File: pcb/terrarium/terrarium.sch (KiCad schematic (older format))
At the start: 11 parts

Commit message: add support for old pcb, add final changes to pcb
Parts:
- added i2c3: Extra_5v, Connector_PinHeader_2.54mm:PinHeader_1x04_P2.54mm_Vertical, symbol Connector_Generic:Conn_01x04
- added i2c4: Extra_3v3, Connector_PinHeader_2.54mm:PinHeader_1x04_P2.54mm_Vertical, symbol Connector_Generic:Conn_01x04
- added rxtx1: Conn_01x02, Connector_PinSocket_2.54mm:PinSocket_1x02_P2.54mm_Vertical, symbol Connector_Generic:Conn_01x02
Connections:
- net 3v3: now also i2c4.2 (Pin_2)
- net GND: now also i2c3.1 (Pin_1), i2c4.1 (Pin_1)
- net SCL: now also i2c3.4 (Pin_4), i2c4.4 (Pin_4)
- net SDA: now also i2c3.3 (Pin_3), i2c4.3 (Pin_3)
- net VCC: now also i2c3.2 (Pin_2)
- net RX: now reaches esp32-left1.15 (Pin_15)
- net RX: now also rxtx1.1 (Pin_1)
- net TX: now reaches esp32-left1.16 (Pin_16)
- net TX: now also rxtx1.2 (Pin_2)
- no-connect marks 34 -> 32
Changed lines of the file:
@@
-$EndComp
-$Comp
-L Connector_Generic:Conn_01x04 i2c2
-U 1 1 618742D4
-P 1550 1950
-F 0 "i2c2" H 1630 1942 50  0000 L CNN
-F 1 "LCD" H 1630 1851 50  0000 L CNN
-F 2 "Connector_PinHeader_2.54mm:PinHeader_1x04_P2.54mm_Vertical" H 1550 1950 50  0001 C CNN
-F 3 "~" H 1550 1950 50  0001 C CNN
-	1    1550 1950
-	1    0    0    -1
 $EndComp
 $Comp
@@
 Text GLabel 1350 1100 0    50   Input ~ 0
 GND
-Text GLabel 1350 1850 0    50   Input ~ 0
-GND
 Text GLabel 3000 3800 0    50   Input ~ 0
 GND
@@
 Text GLabel 2650 1200 0    50   Input ~ 0
 VCC
-Text GLabel 1350 1950 0    50   Input ~ 0
-VCC
 Text GLabel 1350 1200 0    50   Input ~ 0
 3v3
@@
 SDA
 Text GLabel 1350 1400 0    50   Input ~ 0
-SCL
-Text GLabel 1350 2050 0    50   Input ~ 0
-SDA
-Text GLabel 1350 2150 0    50   Input ~ 0
 SCL
 Text GLabel 3000 3600 0    50   Input ~ 0
@@
 NoConn ~ 4500 3700
 NoConn ~ 3000 3700
-NoConn ~ 3000 3500
-NoConn ~ 3000 3400
 NoConn ~ 6700 1400
 NoConn ~ 5700 1400
@@
 Text GLabel 1350 2750 0    50   Input ~ 0
 3v3
+$Comp
+L Connector_Generic:Conn_01x02 rxtx1
+U 1 1 6188472C
+P 1500 4050
+F 0 "rxtx1" H 1580 4042 50  0000 L CNN
+F 1 "Conn_01x02" H 1580 3951 50  0000 L CNN
+F 2 "Connector_PinSocket_2.54mm:PinSocket_1x02_P2.54mm_Vertical" H 1500 4050 50  0001 C CNN
+F 3 "~" H 1500 4050 50  0001 C CNN
+	1    1500 4050
+	1    0    0    -1
+$EndComp
+Text GLabel 1350 2150 0    50   Input ~ 0
+SCL
+Text GLabel 1350 2050 0    50   Input ~ 0
+SDA
+Text GLabel 1350 1950 0    50   Input ~ 0
+VCC
+Text GLabel 1350 1850 0    50   Input ~ 0
+GND
+$Comp
+L Connector_Generic:Conn_01x04 i2c2
+U 1 1 618742D4
+P 1550 1950
+F 0 "i2c2" H 1630 1942 50  0000 L CNN
+F 1 "LCD" H 1630 1851 50  0000 L CNN
+F 2 "Connector_PinHeader_2.54mm:PinHeader_1x04_P2.54mm_Vertical" H 1550 1950 50  0001 C CNN
+F 3 "~" H 1550 1950 50  0001 C CNN
+	1    1550 1950
+	1    0    0    -1
+$EndComp
+Text GLabel 1350 3600 0    50   Input ~ 0
+SCL
+Text GLabel 1350 3500 0    50   Input ~ 0
+SDA
+Text GLabel 1350 3400 0    50   Input ~ 0
+VCC
+Text GLabel 1350 3300 0    50   Input ~ 0
+GND
+$Comp
+L Connector_Generic:Conn_01x04 i2c3
+U 1 1 6188D551
+P 1550 3400
+F 0 "i2c3" H 1630 3392 50  0000 L CNN
+F 1 "Extra_5v" H 1630 3301 50  0000 L CNN
+F 2 "Connector_PinHeader_2.54mm:PinHeader_1x04_P2.54mm_Vertical" H 1550 3400 50  0001 C CNN
+F 3 "~" H 1550 3400 50  0001 C CNN
+	1    1550 3400
+	1    0    0    -1
+$EndComp
+Text GLabel 3000 3500 0    50   Input ~ 0
+TX
+Text GLabel 3000 3400 0    50   Input ~ 0
+RX
+Text GLabel 1300 4050 0    50   Input ~ 0
+RX
+Text GLabel 1300 4150 0    50   Input ~ 0
+TX
+Text GLabel 1350 4800 0    50   Input ~ 0
+SCL
+Text GLabel 1350 4700 0    50   Input ~ 0
+SDA
+Text GLabel 1350 4600 0    50   Input ~ 0
+3v3
+Text GLabel 1350 4500 0    50   Input ~ 0
+GND
+$Comp
+L Connector_Generic:Conn_01x04 i2c4
+U 1 1 6188A3D1
+P 1550 4600
+F 0 "i2c4" H 1630 4592 50  0000 L CNN
+F 1 "Extra_3v3" H 1630 4501 50  0000 L CNN
+F 2 "Connector_PinHeader_2.54mm:PinHeader_1x04_P2.54mm_Vertical" H 1550 4600 50  0001 C CNN
+F 3 "~" H 1550 4600 50  0001 C CNN
+	1    1550 4600
+	1    0    0    -1
+$EndComp
 $EndSCHEMATC

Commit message: wip: relay scheme
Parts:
- added D?: D_Small, symbol Device:D_Small
- added D?: PWR, symbol Device:LED
- added D?: ACTIVE, symbol Device:LED
- added J?: Screw_Terminal_01x03, symbol Connector:Screw_Terminal_01x03
- added K1: SANYOU_SRD_Form_C, Relay_THT:Relay_SPDT_SANYOU_SRD_Series_Form_C, symbol Relay:SANYOU_SRD_Form_C
- added Q?: MMBT3906, Package_TO_SOT_SMD:SOT-23, symbol Transistor_BJT:MMBT3906
- added R? (x3): R_Small, symbol Device:R_Small
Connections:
- net GND: now also D?.1 (K), D?.1 (K), D?.2 (A), K1.2
- net 3v3 renamed +3V3
- net VCC renamed +5V
- net +5V: now also Q?.2 (E), R?.2
- new net: J?.3 (Pin_3), K1.1
- new net: J?.2 (Pin_2), K1.3
- new net: J?.1 (Pin_1), K1.4
- new net: D?.1 (K), K1.5, Q?.3 (C), R?.2
- new net: Q?.1 (B), R?.1
- new net: D?.2 (A), R?.1 (x2)
- new net RELAY3: R?.2
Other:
- moved on the sheet: esp32-right1, relay1, relay2, rxtx1, temp1, temp2, temp3, temp4

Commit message: wip: re-do pcb, add relay
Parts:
- removed D?: D_Small, symbol Device:D_Small
- removed D?: PWR, symbol Device:LED
- removed D?: ACTIVE, symbol Device:LED
- removed J?: Screw_Terminal_01x03, symbol Connector:Screw_Terminal_01x03
- removed K1: SANYOU_SRD_Form_C, Relay_THT:Relay_SPDT_SANYOU_SRD_Series_Form_C, symbol Relay:SANYOU_SRD_Form_C
- removed Q?: MMBT3906, Package_TO_SOT_SMD:SOT-23, symbol Transistor_BJT:MMBT3906
- removed R? (x3): R_Small, symbol Device:R_Small
- added D1: 1N47xxA, Diode_THT:D_DO-41_SOD81_P10.16mm_Horizontal, symbol Diode:1N47xxA
- added D5: ACTIVE, LED_THT:LED_D3.0mm_Clear, symbol Device:LED
- added J3: Screw_Terminal_01x03, Connector_PinSocket_2.54mm:PinSocket_1x03_P2.54mm_Vertical, symbol Connector:Screw_Terminal_01x03
- added K3: SANYOU_SRD_Form_C, Relay_THT:Relay_SPDT_SANYOU_SRD_Series_Form_C, symbol Relay:SANYOU_SRD_Form_C
- added Q2: MMBT3904, Package_TO_SOT_SMD:SOT-23, symbol Transistor_BJT:MMBT3904
- added R5, R6: R_Small, Resistor_THT:R_Axial_DIN0204_L3.6mm_D1.6mm_P2.54mm_Vertical, symbol Device:R_Small
- added U2: MOC3020M, Package_DIP:DIP-6_W7.62mm, symbol Relay_SolidState:MOC3020M
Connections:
- net +5V: now also D1.1 (K), K3.5, U2.6
- net GND: now also D5.1 (K), Q2.2 (E)
- net RELAY3: now also R5.2
- new net: J3.2 (Pin_2), K3.1
- new net: D1.2 (A), K3.2, Q2.3 (C)
- new net: J3.3 (Pin_3), K3.3
- new net: J3.1 (Pin_1), K3.4
- new net: R5.1, U2.1
- new net: D5.2 (A), U2.2
- new net: R6.2, U2.4
- new net: Q2.1 (B), R6.1

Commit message: wip: update pcb
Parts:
- added D2: 1N47xxA, Diode_THT:D_DO-41_SOD81_P7.62mm_Horizontal, symbol Diode:1N47xxA
- added LED2: ACTIVE, LED_THT:LED_D3.0mm_Clear, symbol Device:LED
- added OC2: MOC3020M, Package_DIP:DIP-6_W7.62mm, symbol Relay_SolidState:MOC3020M
- added R3, R4: R_Small, Resistor_THT:R_Axial_DIN0204_L3.6mm_D1.6mm_P2.54mm_Vertical, symbol Device:R_Small
- added RE2: SANYOU_SRD_Form_C, Relay_THT:Relay_SPDT_SANYOU_SRD_Series_Form_C, symbol Relay:SANYOU_SRD_Form_C
- added S2: Screw_Terminal_01x03, Connector_PinSocket_2.54mm:PinSocket_1x03_P2.54mm_Vertical, symbol Connector:Screw_Terminal_01x03
- added TR2: MMBT3904, Package_TO_SOT_THT:TO-92, symbol Transistor_BJT:MMBT3904
- added temp5, temp6: 4, Connector_JST:JST_XH_B3B-XH-AM_1x03_P2.50mm_Vertical, symbol Connector_Generic_MountingPin:Conn_01x03_MountingPin
- D1: footprint Diode_THT:D_DO-41_SOD81_P10.16mm_Horizontal -> Diode_THT:D_DO-41_SOD81_P7.62mm_Horizontal
- TR1: renamed from Q2; footprint Package_TO_SOT_SMD:SOT-23 -> Package_TO_SOT_THT:TO-92
- i2c2: footprint Connector_PinHeader_2.54mm:PinHeader_1x04_P2.54mm_Vertical -> Connector_JST:JST_XH_B4B-XH-AM_1x04_P2.50mm_Vertical
- temp1, temp2, temp3, temp4: footprint Connector_PinHeader_2.54mm:PinHeader_1x03_P2.54mm_Vertical -> Connector_JST:JST_XH_B3B-XH-AM_1x03_P2.50mm_Vertical
- renumbered D5 to LED1, U2 to OC1, R5 to R1, R6 to R2, K3 to RE1, J3 to S1
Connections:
- net RELAY3 is gone; now on net G4: R1.2
- net +5V: now also D2.1 (K), OC2.6, RE2.5, temp5.3 (Pin_3), temp6.3 (Pin_3)
- net G5: now also R3.2
- net GND: now also LED2.1 (K), TR2.2 (E), temp5.1 (Pin_1), temp6.1 (Pin_1)
- net G15: now reaches esp32-left1.4 (Pin_4)
- net G15: now also temp6.2 (Pin_2)
- net G2: now reaches esp32-left1.5 (Pin_5)
- net G2: now also temp5.2 (Pin_2)
- new net: RE2.1, S2.2 (Pin_2)
- new net: D2.2 (A), RE2.2, TR2.3 (C)
- new net: RE2.3, S2.3 (Pin_3)
- new net: RE2.4, S2.1 (Pin_1)
- new net: OC2.1, R3.1
- new net: LED2.2 (A), OC2.2
- new net: OC2.4, R4.2
- new net: R4.1, TR2.1 (B)
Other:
- note added: "DHT22 sensors"
- note added: "esp32"
- note added: "i2c BUS"
- moved on the sheet: D1, ExternalPower1, LED1, OC1, R1, R2, RE1, S1, TR1, esp32-left1, esp32-right1, i2c1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

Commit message: wip: pcb relay design
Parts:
- removed OC1, OC2: MOC3020M, Package_DIP:DIP-6_W7.62mm, symbol Relay_SolidState:MOC3020M
- S1, S2: footprint Connector_PinSocket_2.54mm:PinSocket_1x03_P2.54mm_Vertical -> TerminalBlock:TerminalBlock_bornier-3_P5.08mm
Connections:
- net G4: now also LED1.2 (A); no longer R1.2
- net G5: now also LED2.2 (A); no longer R3.2
- net GND: now also R2.1, R4.1; no longer LED1.1 (K), LED2.1 (K), TR1.2 (E), TR2.2 (E)
- net at R1.1: now also LED1.1 (K)
- net at R2.2: now also TR1.2 (E)
- net at TR1.1 (B): now also R1.2; no longer R2.1
- net at R3.1: now also LED2.1 (K)
- net at R4.2: now also TR2.2 (E)
- net at TR2.1 (B): now also R3.2; no longer R4.1

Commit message: wip: polish pcb
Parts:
- added H1, H2, H3, H4: MountingHole, MountingHole:MountingHole_3.2mm_M3_DIN965_Pad, symbol Mechanical:MountingHole
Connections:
- net GND: now also TR1.2 (E), TR2.2 (E); no longer R2.1, R4.1
- net at R4.2: now also D2.2 (A), RE2.2; no longer TR2.2 (E)
- net at R2.2: now also D1.2 (A), RE1.2; no longer TR1.2 (E)
- net at RE2.4: no longer S2.1 (Pin_1)
- new net: R4.1, TR2.3 (C)
- new net: R2.1, TR1.3 (C)
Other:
- note added: "DIY Relays"
- note added: "Daughter board relays"
- note added: "Mount holes"
- note added: "Utils"
- moved on the sheet: D2, ExternalPower1, LED1, LED2, R1, R2, R3, R4, RE2, S2, TR1, TR2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

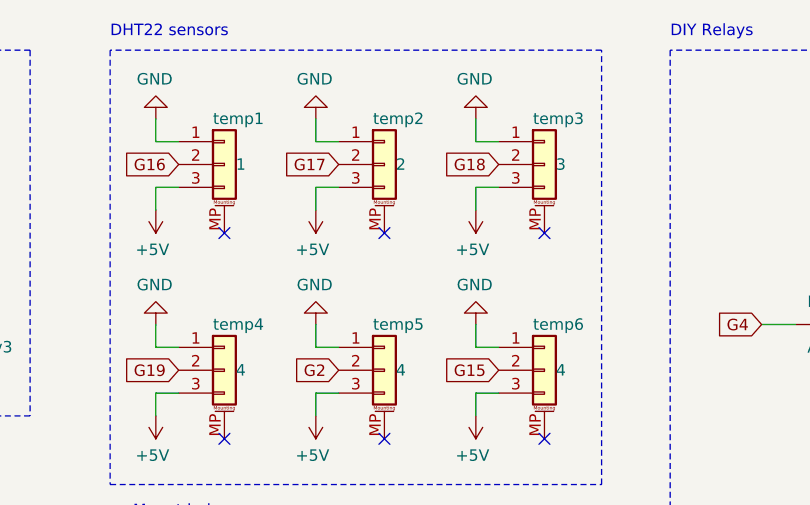
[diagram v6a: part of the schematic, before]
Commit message: fix: gnd connectivity for TR1
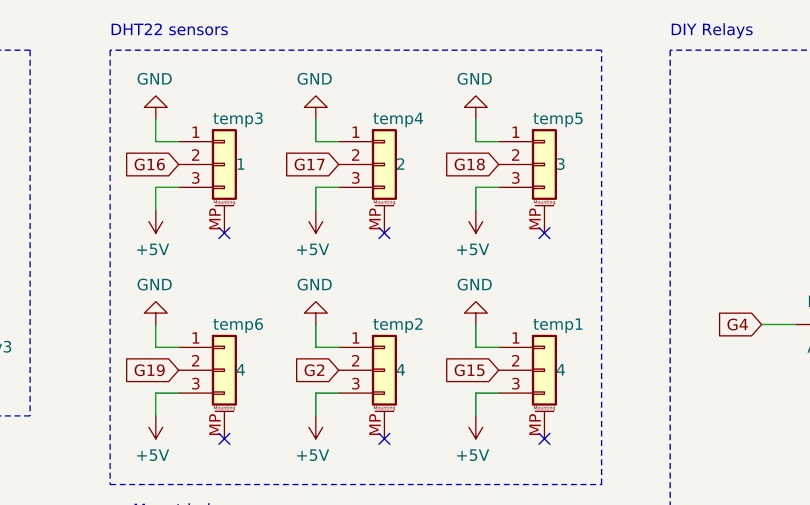
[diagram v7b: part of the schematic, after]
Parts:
- renumbered temp6 to temp1, temp5 to temp2, temp1 to temp3, temp2 to temp4, temp3 to temp5, temp4 to temp6
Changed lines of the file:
@@
 $EndComp
 $Comp
-L Connector_Generic_MountingPin:Conn_01x03_MountingPin temp4
+L Connector_Generic_MountingPin:Conn_01x03_MountingPin temp6
 U 1 1 618718D1
 P 3550 2100
-F 0 "temp4" H 3500 2300 50  0000 L CNN
+F 0 "temp6" H 3500 2300 50  0000 L CNN
 F 1 "4" H 3600 2100 50  0000 L CNN
 F 2 "Connector_JST:JST_XH_B3B-XH-AM_1x03_P2.50mm_Vertical" H 3550 2100 50  0001 C CNN
@@
 $EndComp
 $Comp
-L Connector_Generic_MountingPin:Conn_01x03_MountingPin temp3
+L Connector_Generic_MountingPin:Conn_01x03_MountingPin temp5
 U 1 1 61871FA0
 P 4950 1200
-F 0 "temp3" H 4900 1400 50  0000 L CNN
+F 0 "temp5" H 4900 1400 50  0000 L CNN
 F 1 "3" H 5000 1200 50  0000 L CNN
 F 2 "Connector_JST:JST_XH_B3B-XH-AM_1x03_P2.50mm_Vertical" H 4950 1200 50  0001 C CNN
@@
 $EndComp
 $Comp
-L Connector_Generic_MountingPin:Conn_01x03_MountingPin temp2
+L Connector_Generic_MountingPin:Conn_01x03_MountingPin temp4
 U 1 1 618725D3
 P 4250 1200
-F 0 "temp2" H 4200 1400 50  0000 L CNN
+F 0 "temp4" H 4200 1400 50  0000 L CNN
 F 1 "2" H 4300 1200 50  0000 L CNN
 F 2 "Connector_JST:JST_XH_B3B-XH-AM_1x03_P2.50mm_Vertical" H 4250 1200 50  0001 C CNN
@@
 $EndComp
 $Comp
-L Connector_Generic_MountingPin:Conn_01x03_MountingPin temp1
+L Connector_Generic_MountingPin:Conn_01x03_MountingPin temp3
 U 1 1 61872C21
 P 3550 1200
-F 0 "temp1" H 3500 1400 50  0000 L CNN
+F 0 "temp3" H 3500 1400 50  0000 L CNN
 F 1 "1" H 3600 1200 50  0000 L CNN
 F 2 "Connector_JST:JST_XH_B3B-XH-AM_1x03_P2.50mm_Vertical" H 3550 1200 50  0001 C CNN
@@
 	950  6350 1350 6350
 $Comp
-L Connector_Generic_MountingPin:Conn_01x03_MountingPin temp5
+L Connector_Generic_MountingPin:Conn_01x03_MountingPin temp2
 U 1 1 619D2951
 P 4250 2100
-F 0 "temp5" H 4200 2300 50  0000 L CNN
+F 0 "temp2" H 4200 2300 50  0000 L CNN
 F 1 "4" H 4300 2100 50  0000 L CNN
 F 2 "Connector_JST:JST_XH_B3B-XH-AM_1x03_P2.50mm_Vertical" H 4250 2100 50  0001 C CNN
@@
 	3950 2200 4050 2200
 $Comp
-L Connector_Generic_MountingPin:Conn_01x03_MountingPin temp6
+L Connector_Generic_MountingPin:Conn_01x03_MountingPin temp1
 U 1 1 619D5390
 P 4950 2100
-F 0 "temp6" H 4900 2300 50  0000 L CNN
+F 0 "temp1" H 4900 2300 50  0000 L CNN
 F 1 "4" H 5000 2100 50  0000 L CNN
 F 2 "Connector_JST:JST_XH_B3B-XH-AM_1x03_P2.50mm_Vertical" H 4950 2100 50  0001 C CNN

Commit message: fix: bug with RE2 terminal
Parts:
- renumbered temp3 to HT3, temp4 to HT4, temp5 to HT5
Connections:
- net at RE2.4: now also S2.1 (Pin_1)
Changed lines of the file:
@@
 $EndComp
 $Comp
-L Connector_Generic_MountingPin:Conn_01x03_MountingPin temp6
-U 1 1 618718D1
-P 3550 2100
-F 0 "temp6" H 3500 2300 50  0000 L CNN
-F 1 "4" H 3600 2100 50  0000 L CNN
-F 2 "Connector_JST:JST_XH_B3B-XH-AM_1x03_P2.50mm_Vertical" H 3550 2100 50  0001 C CNN
-F 3 "~" H 3550 2100 50  0001 C CNN
-	1    3550 2100
-	1    0    0    -1
-$EndComp
-$Comp
-L Connector_Generic_MountingPin:Conn_01x03_MountingPin temp5
+L Connector_Generic_MountingPin:Conn_01x03_MountingPin HT5
 U 1 1 61871FA0
 P 4950 1200
-F 0 "temp5" H 4900 1400 50  0000 L CNN
+F 0 "HT5" H 4900 1400 50  0000 L CNN
 F 1 "3" H 5000 1200 50  0000 L CNN
 F 2 "Connector_JST:JST_XH_B3B-XH-AM_1x03_P2.50mm_Vertical" H 4950 1200 50  0001 C CNN
@@
 $EndComp
 $Comp
-L Connector_Generic_MountingPin:Conn_01x03_MountingPin temp4
+L Connector_Generic_MountingPin:Conn_01x03_MountingPin HT4
 U 1 1 618725D3
 P 4250 1200
-F 0 "temp4" H 4200 1400 50  0000 L CNN
+F 0 "HT4" H 4200 1400 50  0000 L CNN
 F 1 "2" H 4300 1200 50  0000 L CNN
 F 2 "Connector_JST:JST_XH_B3B-XH-AM_1x03_P2.50mm_Vertical" H 4250 1200 50  0001 C CNN
@@
 $EndComp
 $Comp
-L Connector_Generic_MountingPin:Conn_01x03_MountingPin temp3
+L Connector_Generic_MountingPin:Conn_01x03_MountingPin HT3
 U 1 1 61872C21
 P 3550 1200
-F 0 "temp3" H 3500 1400 50  0000 L CNN
+F 0 "HT3" H 3500 1400 50  0000 L CNN
 F 1 "1" H 3600 1200 50  0000 L CNN
 F 2 "Connector_JST:JST_XH_B3B-XH-AM_1x03_P2.50mm_Vertical" H 3550 1200 50  0001 C CNN
@@
 Wire Wire Line
 	950  6350 1350 6350
-$Comp
-L Connector_Generic_MountingPin:Conn_01x03_MountingPin temp2
-U 1 1 619D2951
-P 4250 2100
-F 0 "temp2" H 4200 2300 50  0000 L CNN
-F 1 "4" H 4300 2100 50  0000 L CNN
-F 2 "Connector_JST:JST_XH_B3B-XH-AM_1x03_P2.50mm_Vertical" H 4250 2100 50  0001 C CNN
-F 3 "~" H 4250 2100 50  0001 C CNN
-	1    4250 2100
-	1    0    0    -1
-$EndComp
 Text GLabel 4050 2100 0    50   Input ~ 0
 G2
@@
 Wire Wire Line
 	3950 2200 4050 2200
-$Comp
-L Connector_Generic_MountingPin:Conn_01x03_MountingPin temp1
-U 1 1 619D5390
-P 4950 2100
-F 0 "temp1" H 4900 2300 50  0000 L CNN
-F 1 "4" H 5000 2100 50  0000 L CNN
-F 2 "Connector_JST:JST_XH_B3B-XH-AM_1x03_P2.50mm_Vertical" H 4950 2100 50  0001 C CNN
-F 3 "~" H 4950 2100 50  0001 C CNN
-	1    4950 2100
-	1    0    0    -1
-$EndComp
 Text GLabel 4750 2100 0    50   Input ~ 0
 G15
@@
 	8600 3500 8250 3500
 Wire Wire Line
-	8150 2900 8150 2700
-Wire Wire Line
-	8150 2700 9000 2700
-Wire Wire Line
-	8600 2750 9000 2750
-Wire Wire Line
 	8600 2750 8600 3500
 Wire Wire Line
@@
 Text Notes 3150 2750 0    50   ~ 0
 Mount holes
-Connection ~ 8150 2700
-Wire Wire Line
-	8150 2700 8150 2650
 Wire Notes Line
 	5500 700  5500 4400
@@
 Text Notes 700  5700 0    50   ~ 0
 Utils
+Wire Wire Line
+	8600 2750 9000 2750
+$Comp
+L Connector_Generic_MountingPin:Conn_01x03_MountingPin temp1
+U 1 1 619D5390
+P 4950 2100
+F 0 "temp1" H 4900 2300 50  0000 L CNN
+F 1 "4" H 5000 2100 50  0000 L CNN
+F 2 "Connector_JST:JST_XH_B3B-XH-AM_1x03_P2.50mm_Vertical" H 4950 2100 50  0001 C CNN
+F 3 "~" H 4950 2100 50  0001 C CNN
+	1    4950 2100
+	1    0    0    -1
+$EndComp
+$Comp
+L Connector_Generic_MountingPin:Conn_01x03_MountingPin temp2
+U 1 1 619D2951
+P 4250 2100
+F 0 "temp2" H 4200 2300 50  0000 L CNN
+F 1 "4" H 4300 2100 50  0000 L CNN
+F 2 "Connector_JST:JST_XH_B3B-XH-AM_1x03_P2.50mm_Vertical" H 4250 2100 50  0001 C CNN
+F 3 "~" H 4250 2100 50  0001 C CNN
+	1    4250 2100
+	1    0    0    -1
+$EndComp
+$Comp
+L Connector_Generic_MountingPin:Conn_01x03_MountingPin temp6
+U 1 1 618718D1
+P 3550 2100
+F 0 "temp6" H 3500 2300 50  0000 L CNN
+F 1 "4" H 3600 2100 50  0000 L CNN
+F 2 "Connector_JST:JST_XH_B3B-XH-AM_1x03_P2.50mm_Vertical" H 3550 2100 50  0001 C CNN
+F 3 "~" H 3550 2100 50  0001 C CNN
+	1    3550 2100
+	1    0    0    -1
+$EndComp
+Wire Wire Line
+	8150 2900 8150 2650
+Wire Wire Line
+	8150 2650 9000 2650
 $EndSCHEMATC
